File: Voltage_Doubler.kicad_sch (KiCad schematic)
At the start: 11 parts, among them J1 Conn_1x2, J2 Conn_1x2, U1 NE555D

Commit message: updated personal info
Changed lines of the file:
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@@
+	)
+	(junction
+		(at 168.91 92.71)
+		(diameter 0)
+		(color 0 0 0 0)
 	)
 	(junction
@@
 	(wire
 		(pts
+			(xy 162.56 92.71) (xy 168.91 92.71)
+		)
+		(stroke
+			(width 0)
+			(type default)
+		)
+	)
+	(wire
+		(pts
 			(xy 142.24 68.58) (xy 142.24 69.85)
 		)
@@
 	(wire
 		(pts
+			(xy 168.91 92.71) (xy 168.91 91.44)
+		)
+		(stroke
+			(width 0)
+			(type default)
+		)
+	)
+	(wire
+		(pts
 			(xy 123.19 71.12) (xy 123.19 73.66)
 		)
@@
 	(wire
 		(pts
-			(xy 162.56 92.71) (xy 170.18 92.71)
-		)
-		(stroke
+			(xy 170.18 92.71) (xy 168.91 92.71)
+		)
+		(stroke

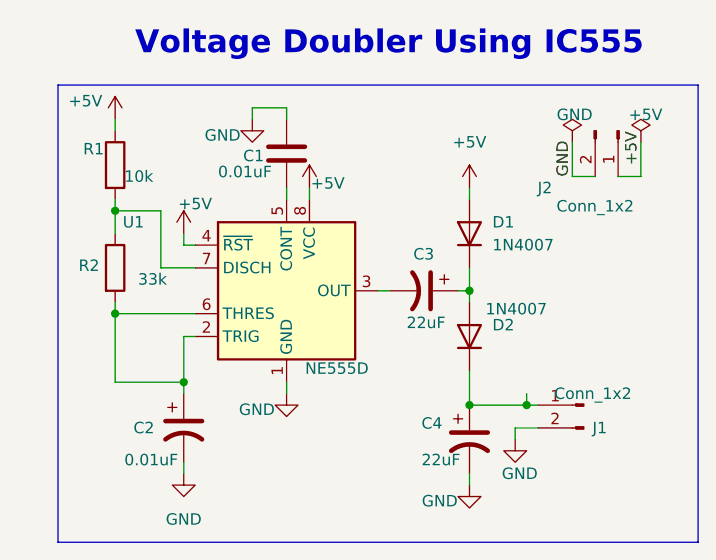
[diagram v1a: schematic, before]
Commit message: Update: added front/back 2D views, copper fill views, schematic view, updated 3D views and PCB/schematic
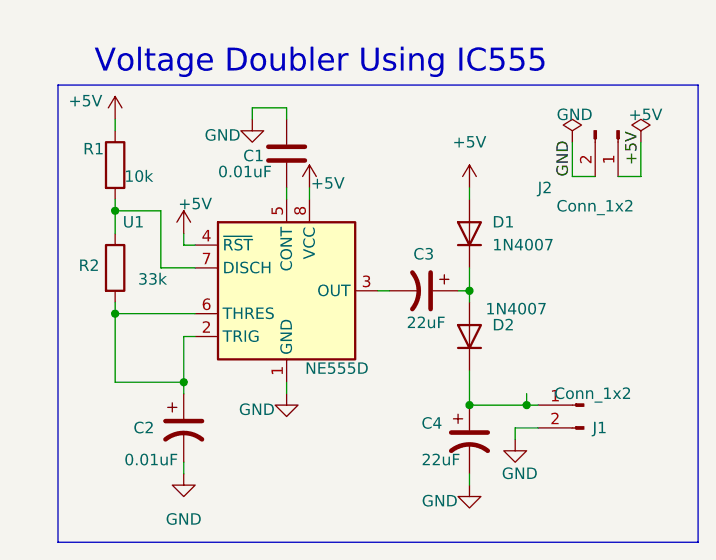
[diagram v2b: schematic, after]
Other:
- company: HighTech -> Ibrahim Jarallah
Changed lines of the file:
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@@
 		(date "2026-02-25")
 		(rev "1.0")
-		(company "HighTech")
+		(company "Ibrahim Jarallah")
 	)
 	(rectangle
@@
 	(text "Voltage Doubler Using IC555"
 		(exclude_from_sim no)
-		(at 153.67 52.578 0)
+		(at 146.05 54.61 0)
 		(effects
 			(font
@@
 				(size 2.54 2.54)
 				(thickness 0.254)
-				(bold yes)
-				(color 69 0 2 1)
+				(color 50 34 69 0.84)
 			)
 		)
